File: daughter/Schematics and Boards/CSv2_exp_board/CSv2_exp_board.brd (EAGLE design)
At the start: 12.5 x 18.3 mm, 115 parts, among them J1 HIROSE-DF40_44-PIN_CONNECTORS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, J3 CORTEX_DEBUG_SMD, J301 HIROSE-DF40_44-PIN_CONNECTORS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, J403 J-WURTH-USBC, J7 J-USB-HIROSE-MICRO-USB, U1 LOADSWITCH-MIC94164, U10 LOADSWITCH-MIC94164, U11 BMI160, U2 ADA4841-1YRJZ-R7, U205 MPL3115A2, U3 Value, U4 RFM69HCW, U5 Value, U6 Value, U7 LOADSWITCH-MIC94164, U8 LOADSWITCH-MIC94164, U9 LOADSWITCH-MIC94164, X1 32.768kHz, X2 32.768, X4 uFL

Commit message: DTR-placement + half manual routing
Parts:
- removed C3: 2.2pF, Capacitors:C0402
- removed C5: 3.9pF, Capacitors:C0402
- removed JP15: JUMPER-SMT_2_NC_PASTE, Connectors:SMT-JUMPER_2_LG_NC_PASTE_NO-SILK
- removed U$7: (no value), microbuilder:ADAFRUIT_3.5MM
- ATT_INT, ATT_SCL, ATT_SDA, BUS0_P0, BUS0_P1, BUS0_P2, BUS0_P3, BUS1_SCL, BUS1_SDA, DTR_DETECT_IN, DTR_DETECT_OUT, EN_BARO, EN_IMU, EN_MEAS, EN_MIC, EN_RADIO, MEAS_BARO, MEAS_IMU, MEAS_MIC, MEAS_RFM, MEAS_SAMD, USBC_V, USB_V: value TPTP14SQ -> TPTP10SQ; device TestPoints:TP14SQ -> TestPoints:TP10SQ
- J2: value (none) -> J-SERIAL-PORT; device Connectors:SCR-3.5MM-3 -> Connectors:HEADER-1X6
- J301: value HIROSE-DF40_44-PIN_CONNECTORS-RECEPTACLE -> HIROSE-DF40_44-PIN_CONNECTORS-HEADER; device Connectors:HRS_DF40HC(3.0)-44DS-0.4V(51) -> Connectors:HRS_DF40C-44DP-0.4V(51)
- JP1, JP10, JP11, JP12, JP13, JP2, JP3, JP4, JP5, JP6, JP7, JP8, JP9: value JUMPER-SMT_2_NC_PASTE -> JUMPER-SMT_2_NC_PASTELG_NO-SILK; device Connectors:SMT-JUMPER_2_LG_NC_PASTE_NO-SILK -> Connectors:SMT-JUMPER_2_NC_PASTE_NO-SILK
- R5, R6: device Resistors:R0805 -> Resistors:R0603
- moved JP17 564.0 mm to (20.7, 35.5), turned to 90 degrees
- moved USB_V 563.6 mm to (12.7, 43.8)
- moved USBC_V 562.7 mm to (20.3, 38.1)
- moved JP19 560.0 mm to (22.2, 35.5), turned to 90 degrees
- moved BUS0_P3 548.8 mm to (26.7, 1.91)
- moved R422 548.2 mm to (24.1, 38.1), turned to 180 degrees
- moved R423 548.2 mm to (27.3, 38.1), turned to 180 degrees
- moved BUS0_P2 544.6 mm to (24.8, 1.91)
- moved J403 544.6 mm to (22.5, 44.8), turned to 180 degrees
- moved BUS0_P1 540.5 mm to (22.9, 1.91)
- moved BUS0_P0 536.3 mm to (21.0, 1.91)
- moved BUS1_SDA 500.0 mm to (35.6, 6.78)
- moved BUS1_SCL 494.7 mm to (35.7, 5.33)
- moved ATT_SDA 489.9 mm to (32.3, 5.05)
- moved ATT_SCL 487.9 mm to (32.3, 6.96)
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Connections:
- net 3V_LD_SW renamed +3V3_SAMD_IN
- net 3V_LD_SW1 renamed +3V3_RFM_IN
- net 3V_LD_SW2 renamed +3V3_BARO_IN
- net 3V_LD_SW3 renamed +3V3_IMU_IN
- net 3V_LD_SW4 renamed +3V3_MIC_IN
- net N$11 renamed +3V3_IMU_PWR
- net N$13 renamed +3V3_BARO_PWR
- net N$14 renamed +3V3_RFM_PWR
- net N$15 renamed +3V3_SAMD_PWR
- net N$16 renamed +3V3_NMEAS
- net N$3 renamed +3V3_MIC_PWR
- net N$4 renamed +3V3_MEAS
- net N0 renamed +3V3_SAMD_OUT
- net N1 renamed +3V3_RFM_OUT
- net N2 renamed +3V3_BARO_OUT
- net N3 renamed +3V3_IMU_OUT
- net N4 renamed +3V3_MIC_OUT
- removed net +3V3: JP12.1, R_SENSE.1
- removed net N$21: J2.3, SJ1.3
- removed net N$24: C3-4.7N.2, JP15.1, R1-100K.1, R3-39R.2
- removed net N$25: C3.2, C5.2, U$1.P
- new net N$3: J2.5, SJ1.3
- net +3V3_DTR: now also JP12.1, R_SENSE.1
- net AT_RESET: now also C3-4.7N.2, R1-100K.1, R3-39R.2; no longer JP15.2
- net GND: now also U$1.G1, U$1.G2; no longer C3.1, C5.1, U$1.GND
- net N$20: now also J2.4; no longer J2.2
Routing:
- net +3V3_DTR: track 0.00 -> 44.2 mm, vias 0 -> 4
- net +3V3_MEAS: track 0.00 -> 39.8 mm, vias 0 -> 6
- net +3V3_NMEAS: track 0.00 -> 39.2 mm, vias 0 -> 6
- net +3V3_DTR0: track 0.00 -> 21.8 mm, vias 0 -> 2
- net GND: track 0.00 -> 14.1 mm, vias 0 -> 2
- net +3V3_ATT: track 0.00 -> 13.3 mm, vias 0 -> 2
- net AT_RESET: track 0.00 -> 12.9 mm
- net VBUS: track 0.00 -> 9.69 mm, vias 0 -> 2
- net +3V3_MIC: track 0.00 -> 9.28 mm, vias 0 -> 1
- net +3V3_IMU: track 0.00 -> 7.78 mm
- net IN+: track 0.00 -> 6.49 mm, vias 0 -> 1
- net +3V3_BARO: track 0.00 -> 6.26 mm
- net SAMD_!RESET: track 0.00 -> 6.19 mm
- net N$23: track 0.00 -> 5.06 mm
- net N$2: track 0.00 -> 5.02 mm
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- added copper zone on layer 15, net GND
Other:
- board size 12.5 x 18.3 mm -> 38.1 x 50.2 mm
- board text removed: "#13"
- board text removed: "10"
- board text removed: "11"
- board text removed: "12"
- board text removed: "13"
- board text removed: "3V"
- board text removed: "5"
- board text removed: "6"
- board text removed: "9"
- board text removed: "A0"
- board text removed: "A1"
- board text removed: "A2"
- board text removed: "A3"
- board text removed: "A4"
- board text removed: "A5"
- board text removed: "ARf"
- board text removed: "BAT"
- board text removed: "CHG"
- board text removed: "En"
- board text removed: "Eve's MEMS Microphone Board v2"
- board text removed: "Feather M0"
- board text removed: "GND"
- board text removed: "MIS"
- board text removed: "MOS"
- board text removed: "Oct. 2019"
- board text removed: "RFM9x LoRa"
- board text removed: "RST"
- board text removed: "RX0"
- board text removed: "Reset"
- board text removed: "SCK"
- board text removed: "SCL"
- board text removed: "SDA"
- board text removed: "TX1"
- board text removed: "USB"
- board text removed: "adafruit!"
- board text removed: "io1"
- board text removed: "~"

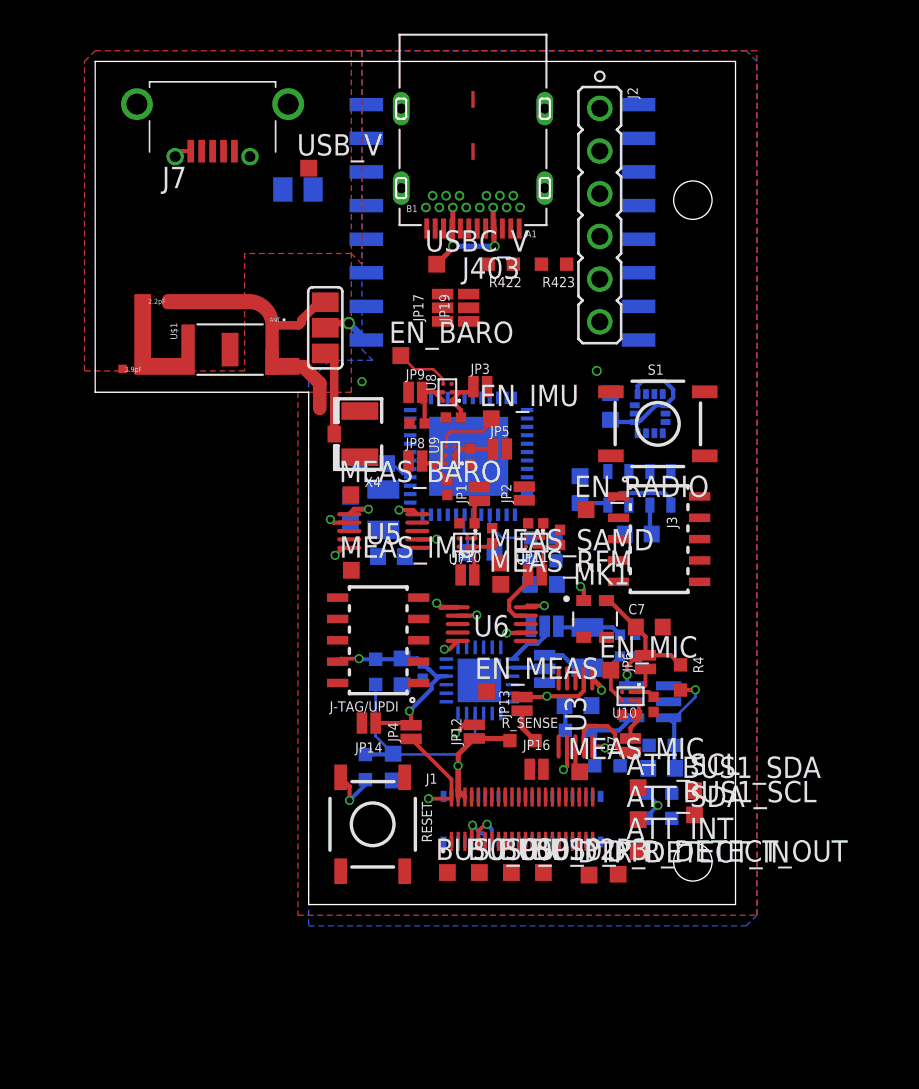
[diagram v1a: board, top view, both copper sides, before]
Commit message: DTR-replacement and manual routing
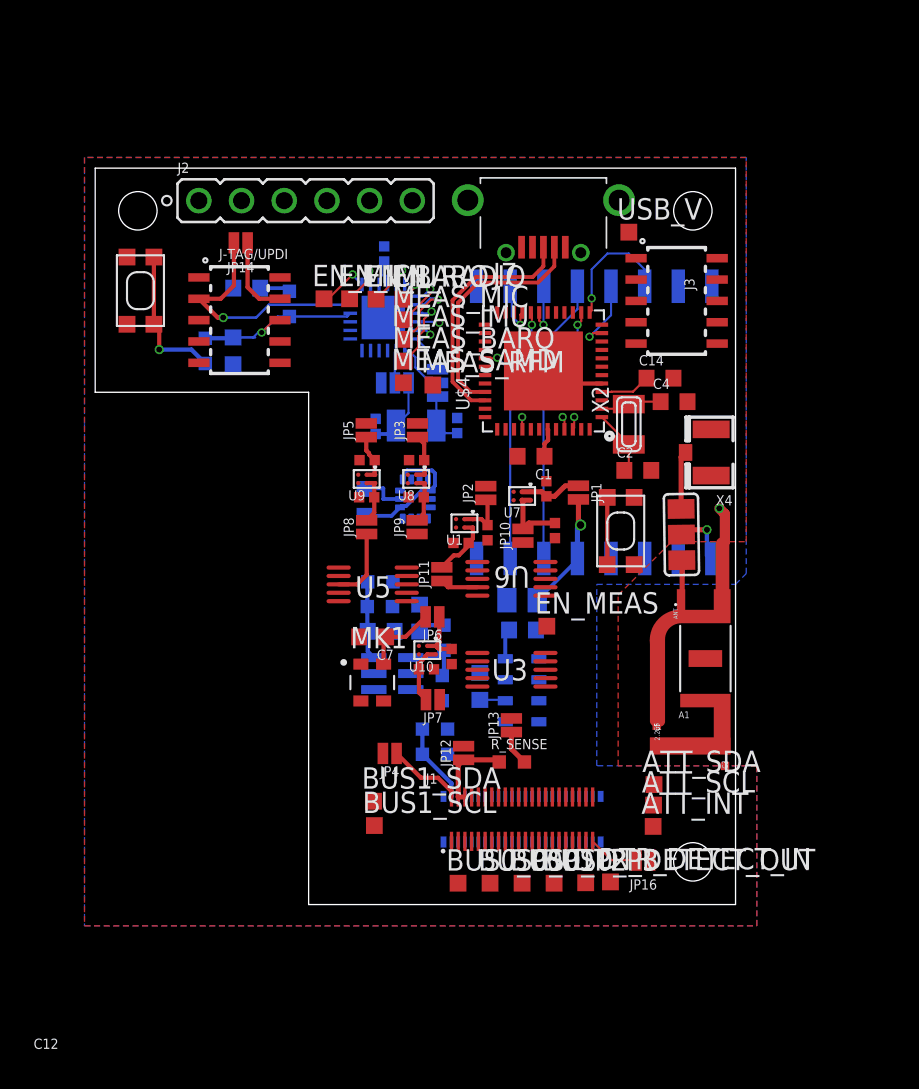
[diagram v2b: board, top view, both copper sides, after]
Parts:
- removed C3-4.7N1: 4.7n, Capacitors:C0603
- removed J403: J-WURTH-USBC, Connectors:632723X00011
- removed JP17, JP19: JUMPER-SMT_3_1-NC_PASTE_NO-SILK, Connectors:SMT-JUMPER_3_1-NC_PASTE_NO-SILK
- removed R1-100K1: 100k, Resistors:R0603
- removed R3-39R1: 39r, Resistors:R0603
- removed R422, R423: 5.1k, Resistors:R0603
- removed RESET, S1: MOMENTARY-SWITCH-SPST-SMD-5.2MM, Switches:TACTILE_SWITCH_SMD_5.2MM
- removed U$1: ILA09_CHIP_ANTENNASMD, CommonSense-DTR-v1:ILA_09_CHIP_ANTENNA
- removed USBC_V: TPTP10SQ, TestPoints:TP10SQ
- added A1: ILA09_CHIP_ANTENNA, CommonSense-DTR-v1:ILA_09_CHIP_ANTENNA2
- added C3: 3.9p, CommonSense-DTR-v1:C0402-S
- added C5: 2.2p, CommonSense-DTR-v1:C0402-S
- added SW1, SW2: SPST_TACT-KMR2, adafruit:KMR2
- moved JP14 29.6 mm to (8.66, 39.4)
- moved MEAS_MIC 28.9 mm to (18.4, 34.8)
- moved EN_MIC 27.9 mm to (13.6, 36.0)
- moved C9 27.8 mm to (25.4, 18.1)
- moved C3-4.7N 26.5 mm to (8.20, 32.9)
- moved R3-39R 26.5 mm to (6.55, 32.9)
- moved C13 24.9 mm to (17.2, 38.7), turned to 270 degrees
- moved C12 24.6 mm to (9.02, 36.7), turned to 180 degrees
- moved SJ3 24.5 mm to (34.9, 22.0), turned to 90.8 degrees
- moved R1-100K 22.5 mm to (11.6, 35.7)
- moved ATTINY-817 22.3 mm to (17.1, 34.9), turned to 270 degrees
- moved X4 20.9 mm to (36.7, 26.9)
- moved J-TAG/UPDI 20.8 mm to (8.59, 34.8), turned to 270 degrees
- moved J7 20.5 mm to (26.7, 41.9)
- moved C4 20.3 mm to (34.4, 29.9), flipped to the top, turned to 0 degrees
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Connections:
- removed net !RESET: R3-39R1.1, S1.3
- removed net CC1: J403.A5, R422.2
- removed net CC2: J403.B5, R423.2
- removed net USBCD_N: J403.A7, J403.B7, JP17.3
- removed net USBCD_P: J403.A6, J403.B6, JP19.3
- removed net USBD_N: J7.D-, JP17.1
- removed net USBD_P: J7.D+, JP19.1
- removed net VBUS: J403.A4, J403.A9, J403.B4, J403.B9, USBC_V.TP
- new net N$4: A1.G2, C3.2, C5.2
- net +3V3_SAMD: no longer R1-100K1.2
- net D_N: now also J7.D-; no longer JP17.2
- net D_P: now also J7.D+; no longer JP19.2
- net GND: now also A1.G1, C3.1, C5.1, SW1.1, SW1.3, SW2.1, SW2.3; no longer C3-4.7N1.1, J403.A1, J403.A12, J403.B1, J403.B12, J403.GND, J403.GND1, J403.Z1, J403.Z2, J403.Z3, J403.Z4, J403.Z5, J403.Z6, R422.1, R423.1, RESET.1, S1.1, U$1.G1, U$1.G2
- net N$12: now also SW1.2, SW1.4; no longer RESET.3
- net SAMD_!RESET: now also SW2.2, SW2.4; no longer C3-4.7N1.2, R1-100K1.1, R3-39R1.2
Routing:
- net +3V3_MEAS: track 39.8 -> 0.00 mm, vias 6 -> 0
- net +3V3_DTR: track 44.2 -> 4.92 mm, vias 4 -> 0
- net +3V3_NMEAS: track 39.2 -> 0.00 mm, vias 6 -> 0
- net LORA_IRQ0: track 0.00 -> 15.6 mm, vias 0 -> 1
- net AT_UPDI: track 0.00 -> 14.7 mm, vias 0 -> 1
- net D_P: track 0.00 -> 14.6 mm
- net D_N: track 0.00 -> 14.2 mm
- net LORA_IRQ1: track 0.00 -> 13.0 mm, vias 0 -> 1
- net +3V3_DTR0: track 21.8 -> 9.26 mm, vias 2 -> 0
- net VBUS: track 9.69 -> 0.00 mm, vias 2 -> 0
- net LORA_RST: track 0.00 -> 7.55 mm, vias 0 -> 1
- net +3V3_RFM: track 0.00 -> 7.12 mm, vias 0 -> 1
- net N$12: track 3.21 -> 9.50 mm
- net LORA_SCK: track 0.00 -> 6.26 mm, vias 0 -> 1
- net +3V3_ATT: track 13.3 -> 8.12 mm, vias 2 -> 0
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- removed copper zone on layer 15, net GND
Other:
- board size 38.1 x 50.2 mm -> 38.1 x 43.8 mm

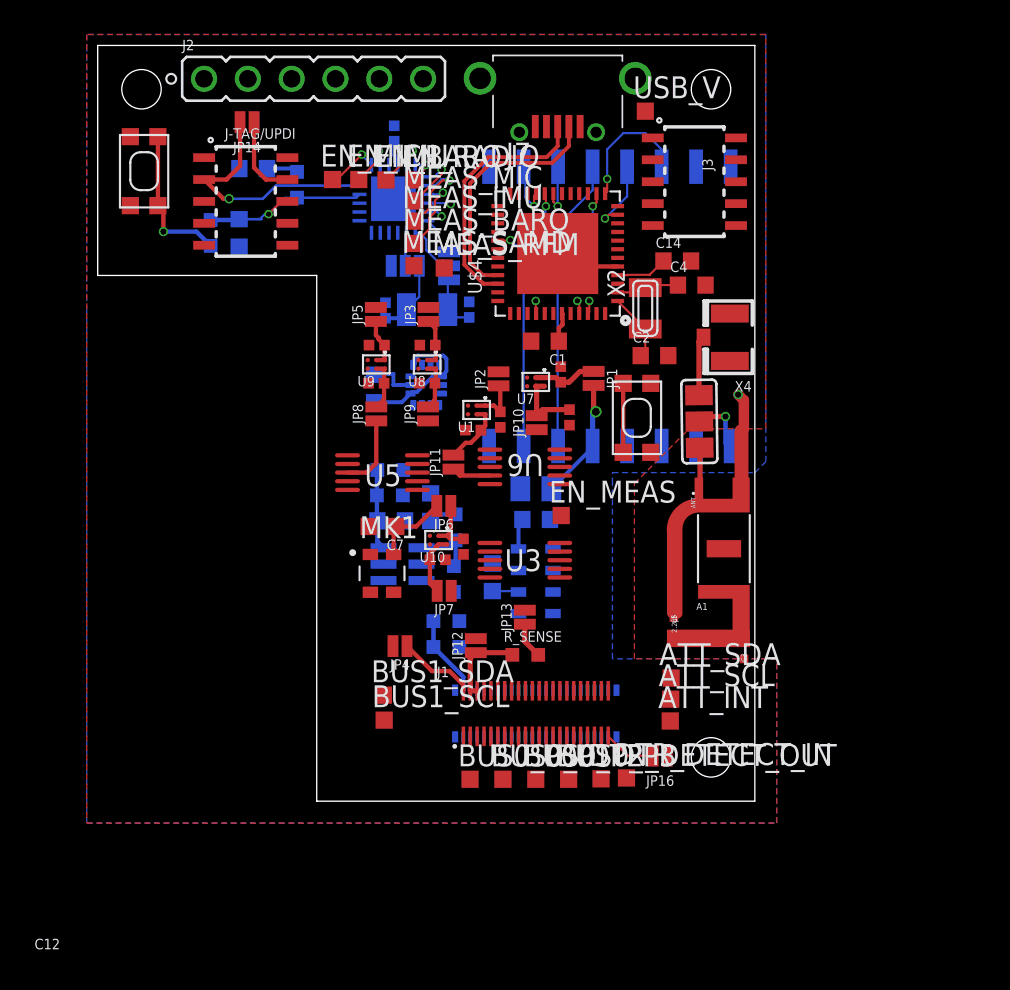
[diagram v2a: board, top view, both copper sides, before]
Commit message: DTR-hand-routing continued
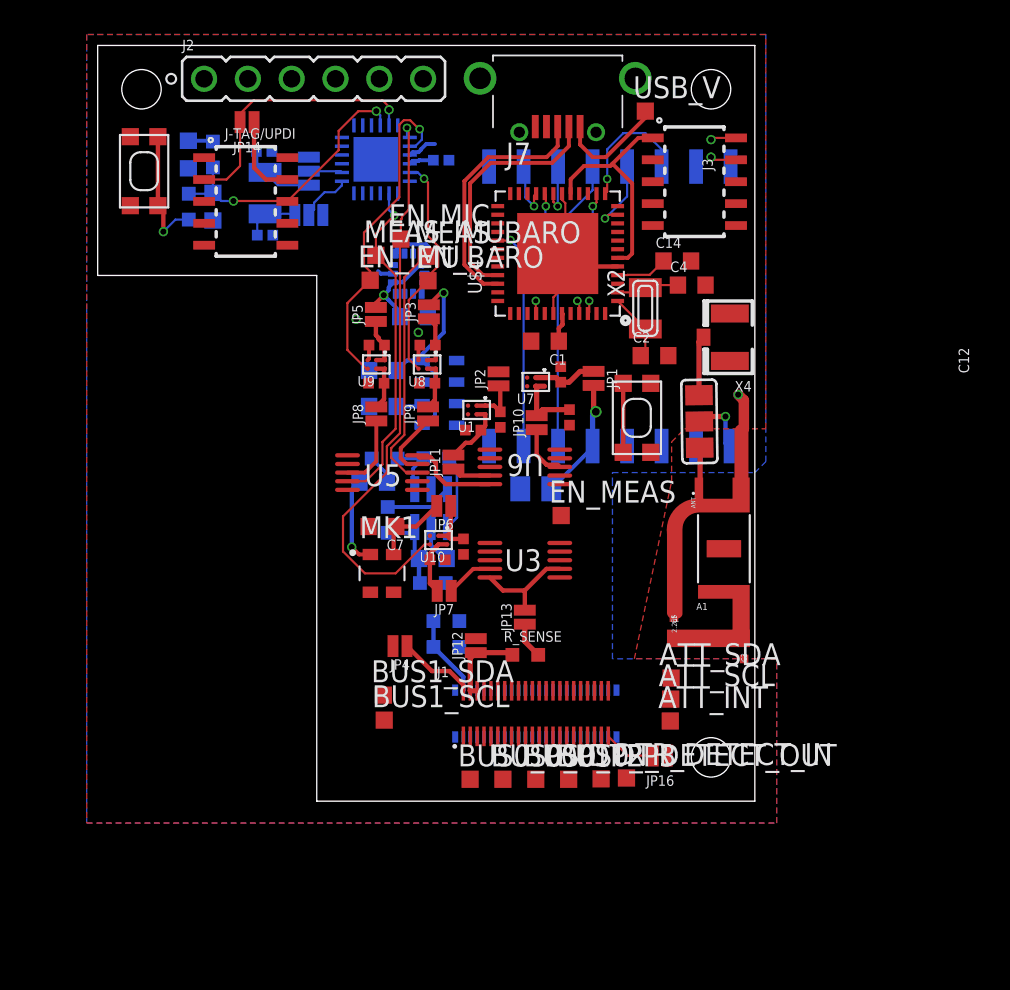
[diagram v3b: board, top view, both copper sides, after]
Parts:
- removed EN_RADIO, MEAS_MIC, MEAS_RFM, MEAS_SAMD: TPTP10SQ, TestPoints:TP10SQ
- moved C16 12.6 mm to (9.70, 32.8), turned to 0 degrees
- moved C203 12.4 mm to (16.5, 25.0), turned to 0 degrees
- moved U205 12.3 mm to (19.8, 23.7)
- moved C204 11.8 mm to (16.5, 22.9), turned to 0 degrees
- moved C15 11.6 mm to (9.65, 37.7), turned to 0 degrees
- moved X1 11.6 mm to (9.70, 35.3), turned to 270 degrees
- moved SJ1 8.65 mm to (12.2, 34.0), turned to 180 degrees
- moved SJ2 7.83 mm to (12.2, 36.5), turned to 90 degrees
- moved R2 7.08 mm to (19.6, 19.9), turned to 0 degrees
- moved U11 6.53 mm to (18.0, 30.6)
- moved EN_BARO 6.33 mm to (19.2, 30.2)
- moved EN_IMU 5.88 mm to (15.8, 30.2)
- moved R1 5.73 mm to (16.6, 19.9), turned to 0 degrees
- moved R3 5.66 mm to (19.4, 12.6)
- moved EN_MIC 5.26 mm to (17.6, 32.6)
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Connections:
- net EN_RADIO: no longer EN_RADIO.TP
- net MEAS_MIC: no longer MEAS_MIC.TP
- net MEAS_RFM: no longer MEAS_RFM.TP
- net MEAS_SAMD: no longer MEAS_SAMD.TP
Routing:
- net EN_MIC: track 3.13 -> 33.8 mm
- net EN_IMU: track 2.97 -> 19.7 mm
- net SWDIO: track 0.76 -> 16.6 mm, vias 1 -> 2
- net MEAS_IMU: track 4.99 -> 20.0 mm
- net +3V3_SAMD: track 0.00 -> 13.2 mm
- net SWCLK: track 0.78 -> 13.8 mm, vias 1 -> 2
- net GND: track 15.9 -> 27.7 mm, vias 1 -> 3
- net +3V3_MEAS: track 0.00 -> 11.3 mm
- net EN_BARO: track 3.32 -> 13.5 mm
- net MEAS_BARO: track 4.56 -> 14.7 mm, vias 1 -> 0
- net +3V3_BARO: track 1.80 -> 11.8 mm, vias 0 -> 1
- net N$17: track 0.00 -> 6.45 mm
- net AT_RESET: track 10.9 -> 16.7 mm, vias 1 -> 2
- net OUT: track 0.00 -> 5.20 mm, vias 0 -> 1
- net BUS0_AIN0: track 0.00 -> 4.41 mm
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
